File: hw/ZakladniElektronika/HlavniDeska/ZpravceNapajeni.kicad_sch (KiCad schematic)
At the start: 7 parts, among them Q10 Q_PMOS_DGS, Q13 Q_PMOS_DGS

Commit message: USB_multiplexer a přehlednost
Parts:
- added R13: 10k, Resistor_SMD:R_0402_1005Metric, symbol Device:R
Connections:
- net 3V3: now also R13.1
- new net DSEL: R13.2
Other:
- sheet Nabijecka ports: added DSEL, I2C, USB; removed CE, D+, D-, INT, QON, SCL, SDA
- sheet Zdroj ports: added EN_ALL, IO_VCC; removed EN-ALL
- moved on the sheet: D?, Q10, Q13, Q?, R13

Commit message: WIP
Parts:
- added TP4: TestPoint-5V_A, symbol Connector:TestPoint
- added TP4: TestPoint-5V, symbol Connector:TestPoint
- added TP4: TestPoint-5V_B, symbol Connector:TestPoint
- added TP4: TestPoint-5V_EN, symbol Connector:TestPoint
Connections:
- net 5V-A: now also TP4.1
- net 5V-B: now also TP4.1
- net NapajeciRozcesti/5V: now also TP4.1
- net NapajeciRozcesti/EN-5V: now also TP4.1
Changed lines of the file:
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@@
 (kicad_sch (version 20230121) (generator eeschema)
   (paper "A4")
+  (junction (at 203.2 38.1) (diameter 0) (color 0 0 0 0)
+  )
   (junction (at 233.68 81.28) (diameter 0) (color 0 0 0 0)
   )
   (junction (at 104.14 139.7) (diameter 0) (color 0 0 0 0)
   )
+  (junction (at 203.2 88.9) (diameter 0) (color 0 0 0 0)
+  )
   (junction (at 233.68 38.1) (diameter 0) (color 0 0 0 0)
   )
   (junction (at 228.6 38.1) (diameter 0) (color 0 0 0 0)
   )
+  (junction (at 254 81.28) (diameter 0) (color 0 0 0 0)
+  )
   (junction (at 104.14 38.1) (diameter 0) (color 0 0 0 0)
   )
@@
   (junction (at 241.3 93.98) (diameter 0) (color 0 0 0 0)
   )
+  (junction (at 254 38.1) (diameter 0) (color 0 0 0 0)
+  )
   (junction (at 241.3 50.8) (diameter 0) (color 0 0 0 0)
   )
@@
     (stroke (width 0) (type default))
   )
+  (wire (pts (xy 88.9 50.8) (xy 92.71 50.8))
+    (stroke (width 0) (type default))
+  )
+  (wire (pts (xy 228.6 38.1) (xy 233.68 38.1))
+    (stroke (width 0) (type default))
+  )
+  (wire (pts (xy 233.68 91.44) (xy 233.68 93.98))
+    (stroke (width 0) (type default))
+  )
+  (wire (pts (xy 124.46 68.58) (xy 124.46 63.5))
+    (stroke (width 0) (type default))
+  )
+  (wire (pts (xy 104.14 35.56) (xy 106.68 35.56))
+    (stroke (width 0) (type default))
+  )
+  (wire (pts (xy 241.3 45.72) (xy 241.3 50.8))
+    (stroke (width 0) (type default))
+  )
+  (wire (pts (xy 91.44 81.28) (xy 91.44 76.2))
+    (stroke (width 0) (type default))
+  )
+  (wire (pts (xy 241.3 93.98) (xy 241.3 96.52))
+    (stroke (width 0) (type default))
+  )
   (wire (pts (xy 254 81.28) (xy 246.38 81.28))
     (stroke (width 0) (type default))
   )
-  (wire (pts (xy 88.9 50.8) (xy 92.71 50.8))
-    (stroke (width 0) (type default))
-  )
-  (wire (pts (xy 228.6 38.1) (xy 233.68 38.1))
-    (stroke (width 0) (type default))
-  )
-  (wire (pts (xy 233.68 91.44) (xy 233.68 93.98))
-    (stroke (width 0) (type default))
-  )
-  (wire (pts (xy 124.46 68.58) (xy 124.46 63.5))
-    (stroke (width 0) (type default))
-  )
-  (wire (pts (xy 104.14 35.56) (xy 106.68 35.56))
-    (stroke (width 0) (type default))
-  )
-  (wire (pts (xy 241.3 45.72) (xy 241.3 50.8))
-    (stroke (width 0) (type default))
-  )
-  (wire (pts (xy 91.44 81.28) (xy 91.44 76.2))
-    (stroke (width 0) (type default))
-  )
-  (wire (pts (xy 241.3 93.98) (xy 241.3 96.52))
-    (stroke (width 0) (type default))
-  )
   (wire (pts (xy 116.84 50.8) (xy 127 50.8))
     (stroke (width 0) (type default))
@@
     (stroke (width 0) (type default))
   )
+  (wire (pts (xy 266.7 81.28) (xy 254 81.28))
+    (stroke (width 0) (type default))
+  )
   (wire (pts (xy 215.9 58.42) (xy 218.44 58.42))
     (stroke (width 0) (type default))
@@
     (stroke (width 0) (type default))
   )
-  (wire (pts (xy 177.8 38.1) (xy 228.6 38.1))
+  (wire (pts (xy 177.8 38.1) (xy 203.2 38.1))
     (stroke (width 0) (type default))
   )
@@
     (stroke (width 0) (type default))
   )
+  (wire (pts (xy 254 38.1) (xy 246.38 38.1))
+    (stroke (width 0) (type default))
+  )
+  (wire (pts (xy 254 81.28) (xy 254 78.74))
+    (stroke (width 0) (type default))
+  )
   (wire (pts (xy 91.44 76.2) (xy 88.9 76.2))
     (stroke (width 0) (type default))
@@
     (stroke (width 0) (type default))
   )
+  (wire (pts (xy 203.2 88.9) (xy 116.84 88.9))
+    (stroke (width 0) (type default))
+  )
   (wire (pts (xy 233.68 93.98) (xy 241.3 93.98))
     (stroke (width 0) (type default))
@@
     (stroke (width 0) (type default))
   )
+  (wire (pts (xy 203.2 86.36) (xy 203.2 88.9))
+    (stroke (width 0) (type default))
+  )
   (wire (pts (xy 104.14 139.7) (xy 127 139.7))
     (stroke (width 0) (type default))
@@
     (stroke (width 0) (type default))
   )
-  (wire (pts (xy 254 38.1) (xy 246.38 38.1))
+  (wire (pts (xy 266.7 38.1) (xy 254 38.1))
+    (stroke (width 0) (type default))
+  )
+  (wire (pts (xy 203.2 35.56) (xy 203.2 38.1))
     (stroke (width 0) (type default))
   )
@@
     (stroke (width 0) (type default))
   )
+  (wire (pts (xy 203.2 38.1) (xy 228.6 38.1))
+    (stroke (width 0) (type default))
+  )
+  (wire (pts (xy 254 38.1) (xy 254 35.56))
+    (stroke (width 0) (type default))
+  )
   (wire (pts (xy 233.68 38.1) (xy 236.22 38.1))
     (stroke (width 0) (type default))
@@
     (stroke (width 0) (type default))
   )
-  (wire (pts (xy 205.74 88.9) (xy 116.84 88.9))
+  (wire (pts (xy 205.74 88.9) (xy 203.2 88.9))
     (stroke (width 0) (type default))
   )
@@
     (effects (font (size 1.27 1.27)) (justify right))
   )
-  (hierarchical_label "5V-A" (shape output) (at 254 38.1 0) (fields_autoplaced)
+  (hierarchical_label "5V-A" (shape output) (at 266.7 38.1 0) (fields_autoplaced)
     (effects (font (size 1.27 1.27)) (justify left))
   )
@@
     (effects (font (size 1.27 1.27)) (justify right))
   )
-  (hierarchical_label "5V-B" (shape output) (at 254 81.28 0) (fields_autoplaced)
+  (hierarchical_label "5V-B" (shape output) (at 266.7 81.28 0) (fields_autoplaced)
     (effects (font (size 1.27 1.27)) (justify left))
   )
@@
     )
   )
+  (symbol (lib_id "Connector:TestPoint") (at 254 35.56 0) (unit 1)
+    (in_bom yes) (on_board yes) (dnp no)
+    (property "Reference" "TP4" (at 255.27 31.75 0)
+      (effects (font (size 1.27 1.27)) (justify left))
+    )
+    (property "Value" "TestPoint-5V_A" (at 255.27 34.29 0)
+      (effects (font (size 1.27 1.27)) (justify left))
+    )
+    (property "Footprint" "" (at 259.08 35.56 0)
+      (effects (font (size 1.27 1.27)) hide)
+    )
+    (property "Datasheet" "~" (at 259.08 35.56 0)
+      (effects (font (size 1.27 1.27)) hide)
+    )
+    (pin "1")
+    (instances
+      (project "ZakladniElektronika"
+        (path "/99cd3e15-4eb6-4cbb-8726-789aedd3df15/c3b70d9b-0dcb-4344-9507-13ff5b4c000e/aae02708-da26-44dd-a602-660fbe003309/fb40dfe9-3eea-4dc3-8528-de588088c9ea"
+          (reference "TP4") (unit 1)
+        )
+        (path "/99cd3e15-4eb6-4cbb-8726-789aedd3df15/c3b70d9b-0dcb-4344-9507-13ff5b4c000e/aae02708-da26-44dd-a602-660fbe003309"
+          (reference "TP11") (unit 1)
+        )
+      )
+    )
+  )
+  (symbol (lib_id "Connector:TestPoint") (at 203.2 35.56 0) (unit 1)
+    (in_bom yes) (on_board yes) (dnp no)
+    (property "Reference" "TP4" (at 201.93 31.75 0)
+      (effects (font (size 1.27 1.27)) (justify right))
+    )
+    (property "Value" "TestPoint-5V" (at 201.93 34.29 0)
+      (effects (font (size 1.27 1.27)) (justify right))
+    )
+    (property "Footprint" "" (at 208.28 35.56 0)
+      (effects (font (size 1.27 1.27)) hide)
+    )
+    (property "Datasheet" "~" (at 208.28 35.56 0)
+      (effects (font (size 1.27 1.27)) hide)
+    )
+    (pin "1")
+    (instances
+      (project "ZakladniElektronika"
+        (path "/99cd3e15-4eb6-4cbb-8726-789aedd3df15/c3b70d9b-0dcb-4344-9507-13ff5b4c000e/aae02708-da26-44dd-a602-660fbe003309/fb40dfe9-3eea-4dc3-8528-de588088c9ea"
+          (reference "TP4") (unit 1)
+        )
+        (path "/99cd3e15-4eb6-4cbb-8726-789aedd3df15/c3b70d9b-0dcb-4344-9507-13ff5b4c000e/aae02708-da26-44dd-a602-660fbe003309"
+          (reference "TP9") (unit 1)
+        )
+      )
+    )
+  )
   (symbol (lib_id "Device:R") (at 104.14 133.35 0) (unit 1)
     (in_bom yes) (on_board yes) (dnp no)
@@
     )
   )
+  (symbol (lib_id "Connector:TestPoint") (at 254 78.74 0) (unit 1)
+    (in_bom yes) (on_board yes) (dnp no)
+    (property "Reference" "TP4" (at 255.27 74.93 0)
+      (effects (font (size 1.27 1.27)) (justify left))
+    )
+    (property "Value" "TestPoint-5V_B" (at 255.27 77.47 0)
+      (effects (font (size 1.27 1.27)) (justify left))
+    )
+    (property "Footprint" "" (at 259.08 78.74 0)
+      (effects (font (size 1.27 1.27)) hide)
+    )
+    (property "Datasheet" "~" (at 259.08 78.74 0)
+      (effects (font (size 1.27 1.27)) hide)
+    )
+    (pin "1")
+    (instances
+      (project "ZakladniElektronika"
+        (path "/99cd3e15-4eb6-4cbb-8726-789aedd3df15/c3b70d9b-0dcb-4344-9507-13ff5b4c000e/aae02708-da26-44dd-a602-660fbe003309/fb40dfe9-3eea-4dc3-8528-de588088c9ea"
+          (reference "TP4") (unit 1)
+        )
+        (path "/99cd3e15-4eb6-4cbb-8726-789aedd3df15/c3b70d9b-0dcb-4344-9507-13ff5b4c000e/aae02708-da26-44dd-a602-660fbe003309"
+          (reference "TP10") (unit 1)
+        )
+      )
+    )
+  )
   (symbol (lib_id "Device:Q_PMOS_DGS") (at 241.3 83.82 270) (mirror x) (unit 1)
     (in_bom yes) (on_board yes) (dnp no)
@@
         )
       )
+    )
+  )
+  (symbol (lib_id "Connector:TestPoint") (at 203.2 86.36 0) (unit 1)
+    (in_bom yes) (on_board yes) (dnp no)
+    (property "Reference" "TP4" (at 201.93 82.55 0)
+      (effects (font (size 1.27 1.27)) (justify right))
+    )
+    (property "Value" "TestPoint-5V_EN" (at 201.93 85.09 0)
+      (effects (font (size 1.27 1.27)) (justify right))
+    )
+    (property "Footprint" "" (at 208.28 86.36 0)
+      (effects (font (size 1.27 1.27)) hide)
+    )
+    (property "Datasheet" "~" (at 208.28 86.36 0)
+      (effects (font (size 1.27 1.27)) hide)
+    )
+    (pin "1")
+    (instances
+      (project "ZakladniElektronika"
+        (path "/99cd3e15-4eb6-4cbb-8726-789aedd3df15/c3b70d9b-0dcb-4344-9507-13ff5b4c000e/aae02708-da26-44dd-a602-660fbe003309/fb40dfe9-3eea-4dc3-8528-de588088c9ea"
+          (reference "TP4") (unit 1)
+        )
+        (path "/99cd3e15-4eb6-4cbb-8726-789aedd3df15/c3b70d9b-0dcb-4344-9507-13ff5b4c000e/aae02708-da26-44dd-a602-660fbe003309"
+          (reference "TP8") (unit 1)
+        )
+      )

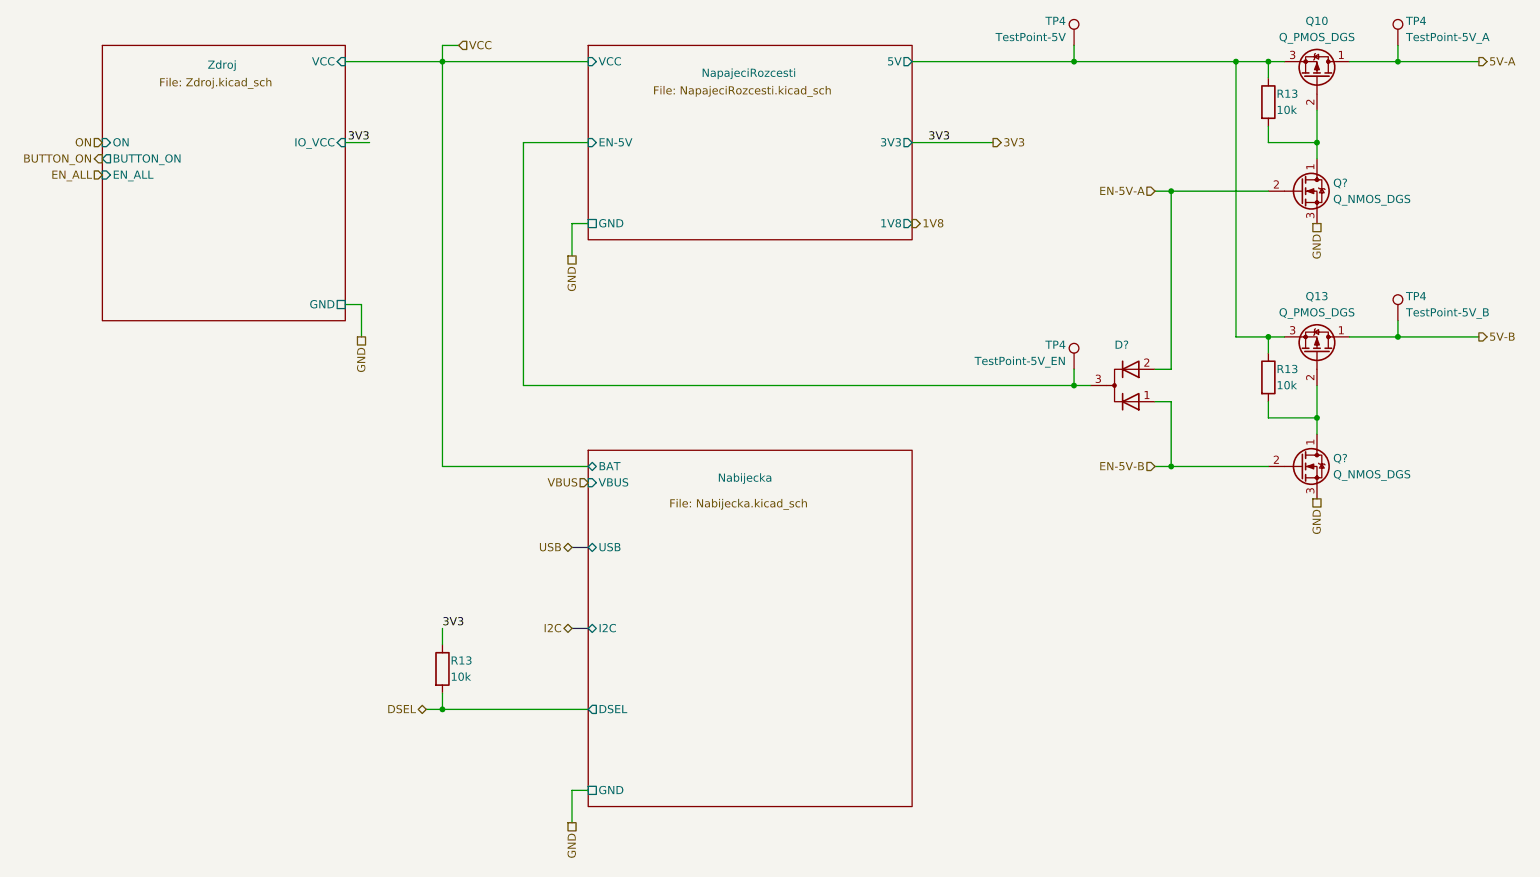
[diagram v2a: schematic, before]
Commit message: Likvidace MiniUI jako samostatné desky a výběr všech komponent
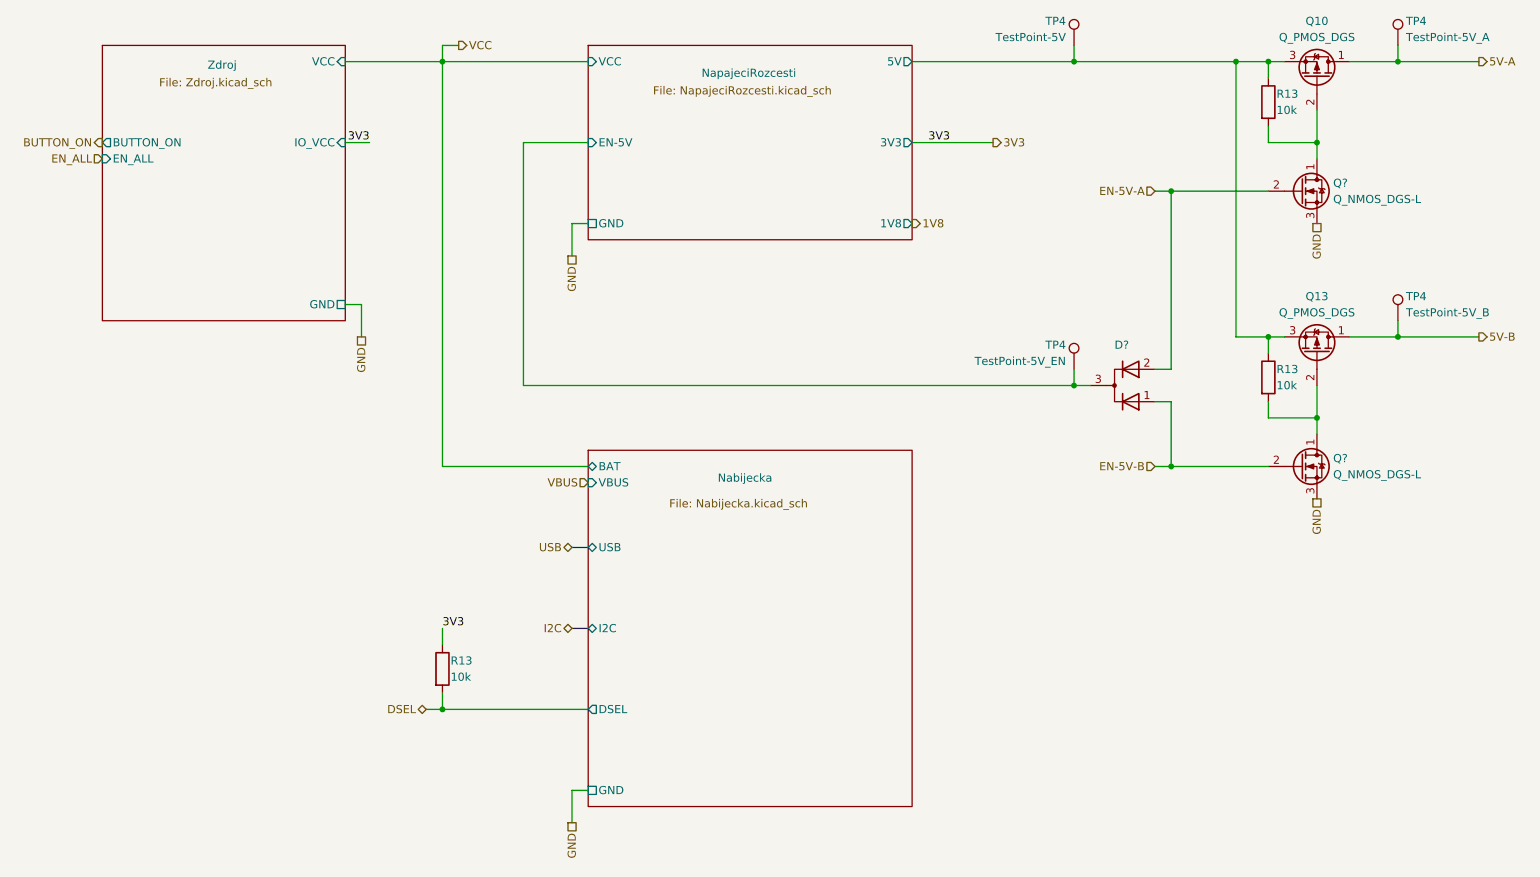
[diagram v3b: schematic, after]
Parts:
- D?: Basic/Extended (none) -> E
- Q10, Q13: footprint RBCX:JMSL0302AU -> Package_SON:Diodes_PowerDI3333-8
- Q? (x2): value Q_NMOS_DGS -> Q_NMOS_DGS-L; Basic/Extended E -> B
- R13: JLCPCB_CORRECTION (none) -> 0;0;0
- TP4: JLCPCB_IGNORE (none) -> ignore
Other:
- sheet Zdroj ports: added none; removed ON
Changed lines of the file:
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@@
     (effects (font (size 1.27 1.27)) (justify left))
   )
-  (hierarchical_label "VCC" (shape input) (at 106.68 35.56 0) (fields_autoplaced)
+  (hierarchical_label "VCC" (shape output) (at 106.68 35.56 0) (fields_autoplaced)
     (effects (font (size 1.27 1.27)) (justify left))
   )
-  (hierarchical_label "EN_ALL" (shape input) (at 50.8 55.88 180) (fields_autoplaced)
+  (hierarchical_label "EN_ALL" (shape input) (at 50.8 53.34 180) (fields_autoplaced)
     (effects (font (size 1.27 1.27)) (justify right))
   )
@@
     (effects (font (size 1.27 1.27)) (justify right))
   )
-  (hierarchical_label "ON" (shape input) (at 50.8 50.8 180) (fields_autoplaced)
-    (effects (font (size 1.27 1.27)) (justify right))
-  )
   (hierarchical_label "5V-B" (shape output) (at 266.7 81.28 0) (fields_autoplaced)
     (effects (font (size 1.27 1.27)) (justify left))
@@
     (effects (font (size 1.27 1.27)) (justify left))
   )
-  (hierarchical_label "BUTTON_ON" (shape output) (at 50.8 53.34 180) (fields_autoplaced)
+  (hierarchical_label "BUTTON_ON" (shape output) (at 50.8 50.8 180) (fields_autoplaced)
     (effects (font (size 1.27 1.27)) (justify right))
   )
@@
       (effects (font (size 1.27 1.27)) hide)
     )
-    (property "Datasheet" "https://datasheet.lcsc.com/lcsc/2210202101_onsemi-DAN222M3T5G_C896182.pdf" (at 209.55 88.9 0)
+    (property "Datasheet" "~" (at 209.55 88.9 0)
       (effects (font (size 1.27 1.27)) hide)
     )
     (property "LCSC" "C896182" (at 210.82 88.9 90)
+      (effects (font (size 1.27 1.27)) hide)
+    )
+    (property "Basic/Extended" "E" (at 210.82 88.9 0)
       (effects (font (size 1.27 1.27)) hide)
     )
@@
       (effects (font (size 1.27 1.27)) hide)
     )
+    (property "JLCPCB_CORRECTION" "0;0;0" (at 233.68 87.63 0)
+      (effects (font (size 1.27 1.27)) hide)
+    )
     (pin "1")
     (pin "2")
@@
       (effects (font (size 1.27 1.27)) hide)
     )
+    (property "JLCPCB_IGNORE" "ignore" (at 254 35.56 0)
+      (effects (font (size 1.27 1.27)) hide)
+    )
     (pin "1")
     (instances
@@
       (effects (font (size 1.27 1.27)) hide)
     )
+    (property "JLCPCB_IGNORE" "ignore" (at 203.2 35.56 0)
+      (effects (font (size 1.27 1.27)) hide)
+    )
     (pin "1")
     (instances
@@
     )
     (property "Basic/Extended" "B" (at 104.14 133.35 0)
+      (effects (font (size 1.27 1.27)) hide)
+    )
+    (property "JLCPCB_CORRECTION" "0;0;0" (at 104.14 133.35 0)
       (effects (font (size 1.27 1.27)) hide)
     )
@@
       (effects (font (size 1.27 1.27)) (justify left))
     )
-    (property "Value" "Q_NMOS_DGS" (at 243.84 102.87 0)
+    (property "Value" "Q_NMOS_DGS-L" (at 243.84 102.87 0)
       (effects (font (size 1.27 1.27)) (justify left))
     )
@@
       (effects (font (size 1.27 1.27)) hide)
     )
-    (property "Datasheet" "https://datasheet.lcsc.com/lcsc/1808272021_Vishay-Intertech-SI2301CDS-T1-GE3_C10487.pdf" (at 238.76 101.6 0)
+    (property "Datasheet" "~" (at 238.76 101.6 0)
       (effects (font (size 1.27 1.27)) hide)
     )
@@
       (effects (font (size 1.27 1.27)) hide)
     )
-    (property "Basic/Extended" "E" (at 238.76 101.6 0)
+    (property "Basic/Extended" "B" (at 238.76 101.6 0)
       (effects (font (size 1.27 1.27)) hide)
     )
@@
       (effects (font (size 1.27 1.27)) hide)
     )
+    (property "JLCPCB_CORRECTION" "0;0;0" (at 233.68 44.45 0)
+      (effects (font (size 1.27 1.27)) hide)
+    )
     (pin "1")
     (pin "2")
@@
       (effects (font (size 1.27 1.27)) hide)
     )
+    (property "JLCPCB_IGNORE" "ignore" (at 254 78.74 0)
+      (effects (font (size 1.27 1.27)) hide)
+    )
     (pin "1")
     (instances
@@
       (effects (font (size 1.27 1.27)))
     )
-    (property "Footprint" "RBCX:JMSL0302AU" (at 243.84 78.74 0)
+    (property "Footprint" "Package_SON:Diodes_PowerDI3333-8" (at 243.84 78.74 0)
       (effects (font (size 1.27 1.27)) hide)
     )
@@
       (effects (font (size 1.27 1.27)))
     )
-    (property "Footprint" "RBCX:JMSL0302AU" (at 243.84 35.56 0)
+    (property "Footprint" "Package_SON:Diodes_PowerDI3333-8" (at 243.84 35.56 0)
       (effects (font (size 1.27 1.27)) hide)
     )
@@
       (effects (font (size 1.27 1.27)) hide)
     )
+    (property "JLCPCB_IGNORE" "ignore" (at 203.2 86.36 0)
+      (effects (font (size 1.27 1.27)) hide)
+    )
     (pin "1")
     (instances
@@
       (effects (font (size 1.27 1.27)) (justify left))
     )
-    (property "Value" "Q_NMOS_DGS" (at 243.84 59.69 0)
+    (property "Value" "Q_NMOS_DGS-L" (at 243.84 59.69 0)
       (effects (font (size 1.27 1.27)) (justify left))
     )
@@
       (effects (font (size 1.27 1.27)) hide)
     )
-    (property "Datasheet" "https://datasheet.lcsc.com/lcsc/1808272021_Vishay-Intertech-SI2301CDS-T1-GE3_C10487.pdf" (at 238.76 58.42 0)
+    (property "Datasheet" "~" (at 238.76 58.42 0)
       (effects (font (size 1.27 1.27)) hide)
     )
@@
       (effects (font (size 1.27 1.27)) hide)
     )
-    (property "Basic/Extended" "E" (at 238.76 58.42 0)
+    (property "Basic/Extended" "B" (at 238.76 58.42 0)
       (effects (font (size 1.27 1.27)) hide)
     )
@@
       (effects (font (size 1.27 1.27)) (justify right))
     )
-    (pin "ON" input (at 50.8 50.8 180)
-      (effects (font (size 1.27 1.27)) (justify left))
-    )
-    (pin "BUTTON_ON" output (at 50.8 53.34 180)
-      (effects (font (size 1.27 1.27)) (justify left))
-    )
-    (pin "EN_ALL" input (at 50.8 55.88 180)
-      (effects (font (size 1.27 1.27)) (justify left))
-    )
+    (pin "BUTTON_ON" output (at 50.8 50.8 180)
+      (effects (font (size 1.27 1.27)) (justify left))
+    )
+    (pin "EN_ALL" input (at 50.8 53.34 180)
+      (effects (font (size 1.27 1.27)) (justify left))
+    )
